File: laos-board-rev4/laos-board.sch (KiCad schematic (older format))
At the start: 101 parts, among them IC1 KB847, IC2 KB847, J1 USB-A, J10 I2C, J11 MBED NXP, J12 JP, J13 ZEXT, J14 ANALOG, J15 JP, J16 JP_3, J17 POLOLU1201, J18 YAXIS, J19 JP, J2 CAN, J20 YEXT, J21 JP, J22 JP_3, J23 POLOLU1201, J24 XAXIS, J25 JP, J26 XEXT, J27 OUTPUT, J28 VSENSOR, J29 INPUT12, J3 USBPWR, J30 JP, J31 JP_3, J32 POLOLU1201, J33 EAXIS, J34 INPUT34, J35 JP, J36 EEXT, J37 OUTPUT12, J38 VCPU, J39 OUTPUT34, J4 MAGJACK, J40 JP, J41 O1_SRC, J42 O2_SRC, J43 CONN_4, J44 JP, J5 CONN_3, J6 JP, J7 JP_3, J8 POLOLU1201, J9 ZAXIS, P1 FLATCONN, Q1 TIP115, Q2 TIP115, U1 65HVD251, U2 SDCARD, U3 7805, U4 MCP1703

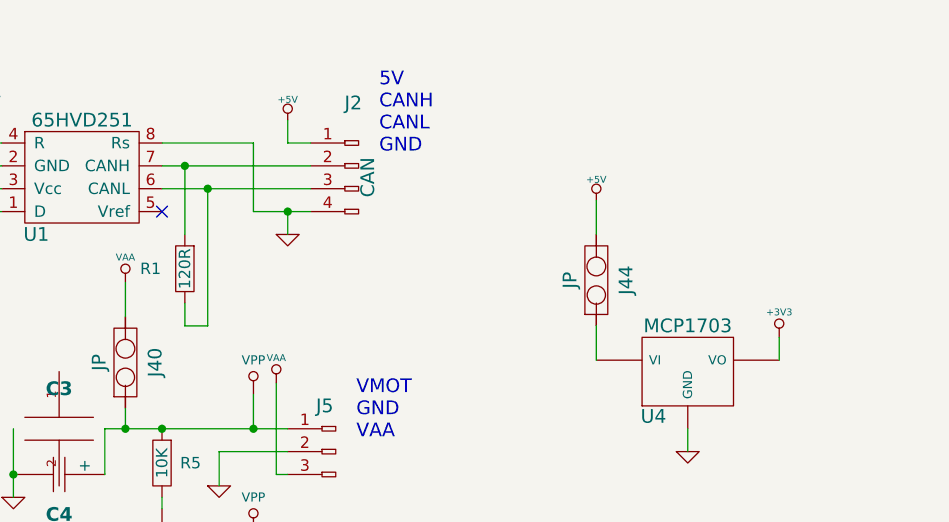
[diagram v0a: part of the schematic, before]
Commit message: added RJ12 for CAN
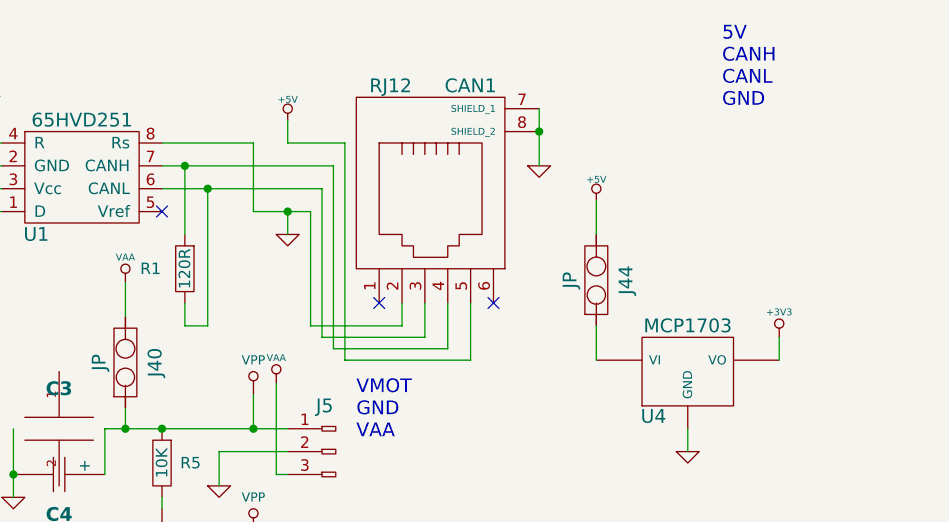
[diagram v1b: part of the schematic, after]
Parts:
- removed J2: CAN, Pkg, symbol CONN_4
- added CAN1: RJ12, symbol RJ12
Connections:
- net +5V: now also CAN1.5
- net GND: now also CAN1.2, CAN1.7 (SHIELD_1), CAN1.8 (SHIELD_2)
- net at R1.2, U1.7 (CANH): now also CAN1.4
- net at R1.1, U1.6 (CANL): now also CAN1.3
- no-connect marks 9 -> 11

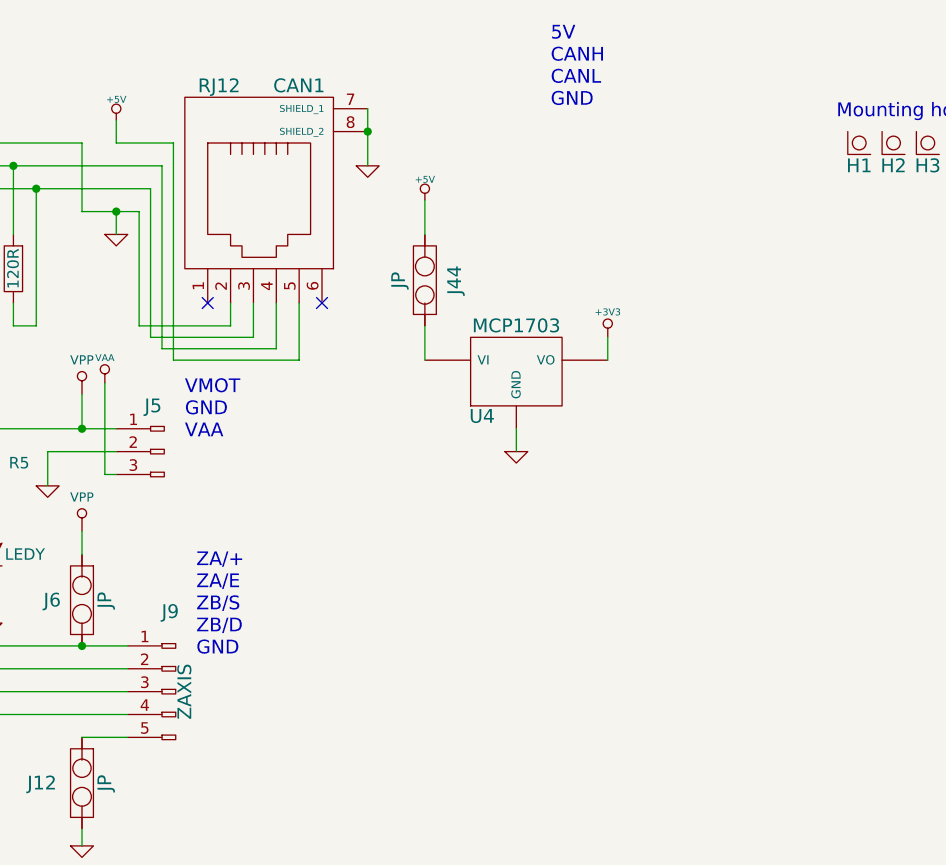
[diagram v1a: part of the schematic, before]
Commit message: updated CAN connector + thicker powerlines
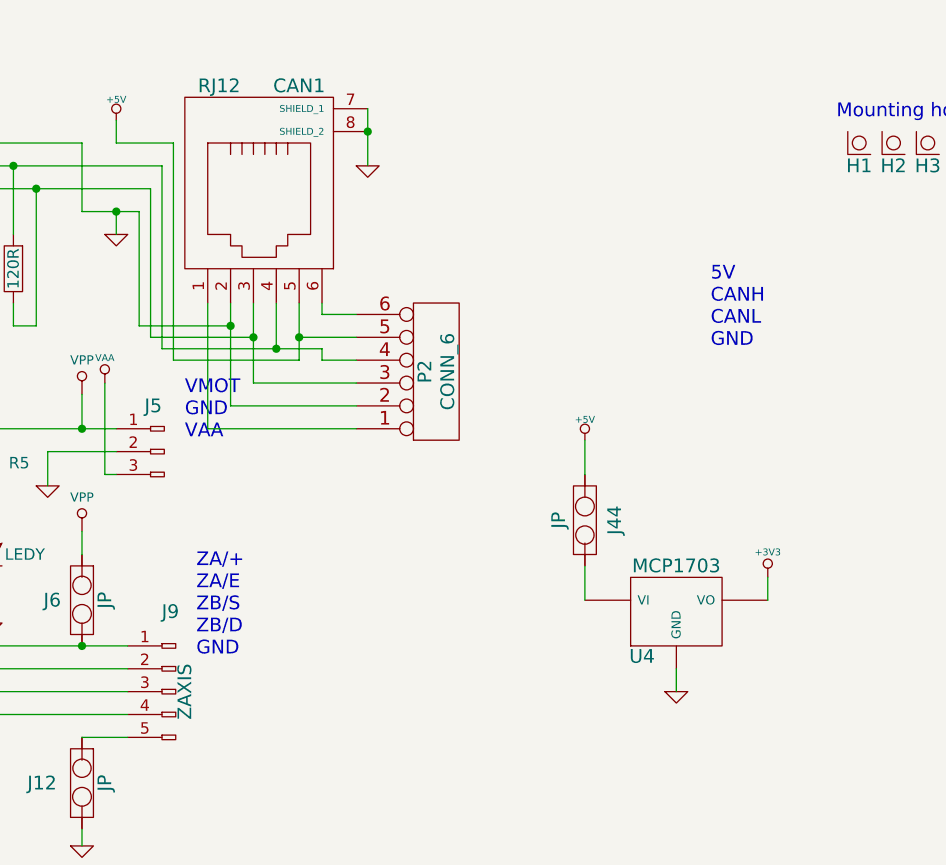
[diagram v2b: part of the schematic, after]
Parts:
- added P2: CONN_6, symbol CONN_6
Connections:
- net +5V: now also P2.5
- net GND: now also P2.2
- net at CAN1.3, R1.1, U1.6 (CANL): now also P2.3
- net at CAN1.4, R1.2, U1.7 (CANH): now also P2.4
- net at CAN1.1: now also P2.1
- net at CAN1.6: now also P2.6
- no-connect marks 11 -> 9
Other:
- moved on the sheet: J44, U4
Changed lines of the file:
@@
-EESchema Schematic File Version 2  date Sun 30 Sep 2012 06:13:09 PM CEST
+EESchema Schematic File Version 2  date Mon 01 Oct 2012 11:29:24 AM CEST
 LIBS:laos_kicad_lib
 LIBS:power
@@
 Sheet 1 1
 Title "LAOS"
-Date ""
+Date "1 oct 2012"
 Rev "4"
 Comp "http://www.laoslaser.org"
@@
 Comment4 ""
 $EndDescr
-NoConn ~ 13050 1500
-NoConn ~ 12550 1500
+Wire Wire Line
+	12550 1500 12550 2050
+Wire Wire Line
+	12550 2050 13200 2050
+Connection ~ 12950 1650
+Wire Wire Line
+	13200 1650 12950 1650
+Connection ~ 12750 1650
+Wire Wire Line
+	13200 1850 12750 1850
+Wire Wire Line
+	12750 1850 12750 1500
 Connection ~ 13250 750
 Wire Wire Line
@@
 	12400 800  12150 800
 Wire Wire Line
-	12750 1500 12750 1650
-Wire Wire Line
 	12750 1650 12300 1650
 Wire Wire Line
@@
 	12300 1000 11600 1000
 Wire Wire Line
-	13500 1600 13500 1750
-Wire Wire Line
-	14300 1750 14300 1650
-Wire Wire Line
-	13900 2050 13900 2150
+	14200 2650 14200 2800
+Wire Wire Line
+	15000 2800 15000 2700
+Wire Wire Line
+	14600 3100 14600 3200
 Wire Wire Line
 	6900 5300 6900 9975
@@
 	6700 5100 6600 5100
 Wire Wire Line
-	13500 1050 13500 1200
+	14200 2100 14200 2250
 Wire Wire Line
 	12250 1100 12250 1600
@@
 	12250 1600 12650 1600
 Wire Wire Line
-	12650 1600 12650 1500
-Wire Wire Line
-	12350 1700 12850 1700
-Wire Wire Line
 	12850 1700 12850 1500
+Wire Wire Line
+	13050 1500 13050 1550
+Wire Wire Line
+	13050 1550 13200 1550
+Wire Wire Line
+	12650 1500 12650 1950
+Wire Wire Line
+	12650 1950 13200 1950
+Connection ~ 12650 1600
+Wire Wire Line
+	12350 1700 13050 1700
+Wire Wire Line
+	13050 1700 13050 1750
+Wire Wire Line
+	13050 1750 13200 1750
+Connection ~ 12850 1700
+$Comp
+L CONN_6 P2
+U 1 1 506966F5
+P 13550 1800
+F 0 "P2" V 13500 1800 60  0000 C CNN
+F 1 "CONN_6" V 13600 1800 60  0000 C CNN
+	1    13550 1800
+	1    0    0    1
+$EndComp
 $Comp
 L GND #PWR01
@@
 L JP J44
 U 1 1 506860C5
-P 13500 1400
-F 0 "J44" H 13500 1270 60  0000 C CNN
-F 1 "JP" H 13500 1515 60  0000 C CNN
-	1    13500 1400
+P 14200 2450
+F 0 "J44" H 14200 2320 60  0000 C CNN
+F 1 "JP" H 14200 2565 60  0000 C CNN
+	1    14200 2450
 	0    -1   -1   0
 $EndComp
@@
 L GND #PWR02
 U 1 1 50686104
-P 13900 2150
-F 0 "#PWR02" H 13900 2150 30  0001 C CNN
-F 1 "GND" H 13900 2080 30  0001 C CNN
-	1    13900 2150
+P 14600 3200
+F 0 "#PWR02" H 14600 3200 30  0001 C CNN
+F 1 "GND" H 14600 3130 30  0001 C CNN
+	1    14600 3200
 	1    0    0    -1
 $EndComp
@@
 L MCP1703 U4
 U 1 1 506860E1
-P 13900 1750
-F 0 "U4" H 13750 1504 60  0000 C CNN
-F 1 "MCP1703" H 13900 1900 60  0000 C CNN
-	1    13900 1750
+P 14600 2800
+F 0 "U4" H 14450 2554 60  0000 C CNN
+F 1 "MCP1703" H 14600 2950 60  0000 C CNN
+	1    14600 2800
 	1    0    0    -1
 $EndComp
@@
 L +3V3 #PWR03
 U 1 1 50685E65
-P 14300 1650
-F 0 "#PWR03" H 14300 1610 30  0001 C CNN
-F 1 "+3V3" H 14300 1760 30  0000 C CNN
-	1    14300 1650
+P 15000 2700
+F 0 "#PWR03" H 15000 2660 30  0001 C CNN
+F 1 "+3V3" H 15000 2810 30  0000 C CNN
+	1    15000 2700
 	1    0    0    -1
 $EndComp
@@
 L +5V #PWR04
 U 1 1 50685366
-P 13500 1050
-F 0 "#PWR04" H 13500 1140 20  0001 C CNN
-F 1 "+5V" H 13500 1140 30  0000 C CNN
-	1    13500 1050
+P 14200 2100
+F 0 "#PWR04" H 14200 2190 20  0001 C CNN
+F 1 "+5V" H 14200 2190 30  0000 C CNN
+	1    14200 2100
 	1    0    0    -1
 $EndComp
@@
 	-1   0    0    1
 $EndComp
-Text Notes 14050 650  0    60   ~ 0
+Text Notes 14750 1700 0    60   ~ 0
 5V\nCANH\nCANL\nGND
 $Comp

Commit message: replaced 3v3 voltage regulator, added capacitors for Pololu decoupling
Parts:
- removed U4: MCP1703, symbol MCP1703
- added C10, C11, C9: 100uF, Pkg, symbol CAP_POL
- added C13, C14: 22nF, symbol CAP
- added U4: SP6205, symbol TPS769XX
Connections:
- net +3V3: now also C13.1, U4.5 (OUT)
- net GND: now also C10.2, C11.2, C13.2, C14.2, C9.2, U4.2 (GND)
- net VPP: now also C10.1 (+), C11.1 (+), C9.1 (+)
- net at J44.1: now also C14.1, U4.1 (IN)
- no-connect marks 9 -> 11
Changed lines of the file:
@@
-EESchema Schematic File Version 2  date Mon 01 Oct 2012 11:29:24 AM CEST
+EESchema Schematic File Version 2  date Tue 02 Oct 2012 08:27:16 PM CEST
 LIBS:laos_kicad_lib
 LIBS:power
@@
 Sheet 1 1
 Title "LAOS"
-Date "1 oct 2012"
+Date "2 oct 2012"
 Rev "4"
 Comp "http://www.laoslaser.org"
@@
 $EndDescr
 Wire Wire Line
+	10050 8025 10300 8025
+Wire Wire Line
+	10050 8625 10150 8625
+Wire Wire Line
+	10050 6800 10150 6800
+Connection ~ 10300 4450
+Wire Wire Line
+	10050 4450 10700 4450
+Wire Wire Line
+	10700 4450 10700 5150
+Wire Wire Line
+	10050 3400 10150 3400
+Connection ~ 14650 3350
+Connection ~ 15350 2800
+Wire Wire Line
+	15350 2700 15350 2850
+Wire Wire Line
+	13900 2850 13900 2800
+Wire Wire Line
 	12550 1500 12550 2050
 Wire Wire Line
@@
 Wire Wire Line
 	14200 2650 14200 2800
-Wire Wire Line
-	15000 2800 15000 2700
-Wire Wire Line
-	14600 3100 14600 3200
 Wire Wire Line
 	6900 5300 6900 9975
@@
 	11850 2150 12150 2150
 Wire Wire Line
-	10300 7850 10300 8025
+	10300 8025 10300 7850
 Wire Wire Line
 	12000 5900 12000 6000
@@
 	8250 8725 9300 8725
 Wire Wire Line
-	10050 8625 10150 8625
-Wire Wire Line
 	9200 8425 9300 8425
 Wire Wire Line
@@
 Connection ~ 8750 8325
 Wire Wire Line
-	10300 8025 10050 8025
-Wire Wire Line
 	10050 8125 10300 8125
 Wire Wire Line
@@
 Wire Wire Line
 	10300 6300 10050 6300
-Wire Wire Line
-	10050 6200 10300 6200
 Connection ~ 8750 6500
 Wire Wire Line
@@
 	8150 6400 8100 6400
 Wire Wire Line
-	10150 6100 10150 6800
+	10150 6800 10150 6100
 Wire Wire Line
 	9300 6600 9200 6600
-Wire Wire Line
-	10150 6800 10050 6800
 Wire Wire Line
 	9300 6700 9200 6700
@@
 	9200 4950 9300 4950
 Wire Wire Line
-	10050 5050 10150 5050
-Wire Wire Line
 	9200 4850 9300 4850
 Wire Wire Line
-	10150 5050 10150 4350
+	10150 4350 10150 5050
 Wire Wire Line
 	8150 4650 8100 4650
@@
 Connection ~ 8750 4750
 Wire Wire Line
-	10050 4450 10300 4450
-Wire Wire Line
 	10300 4450 10300 4350
 Wire Wire Line
@@
 	10300 2900 10050 2900
 Wire Wire Line
-	10300 2700 10300 2800
-Wire Wire Line
-	10300 2800 10050 2800
+	10300 2800 10300 2700
 Connection ~ 8750 3100
 Wire Wire Line
@@
 	8150 3000 8100 3000
 Wire Wire Line
-	10150 2700 10150 3400
+	10150 3400 10150 2700
 Wire Wire Line
 	9300 3200 9200 3200
-Wire Wire Line
-	10150 3400 10050 3400
 Wire Wire Line
 	9300 3300 9200 3300
@@
 	13050 1750 13200 1750
 Connection ~ 12850 1700
+Wire Wire Line
+	14200 2800 13900 2800
+Wire Wire Line
+	15350 2800 15100 2800
+Wire Wire Line
+	14650 3250 14650 3550
+Wire Wire Line
+	13900 3350 15350 3350
+Wire Wire Line
+	10700 3500 10700 2800
+Wire Wire Line
+	10700 2800 10050 2800
+Connection ~ 10300 2800
+Wire Wire Line
+	10150 5050 10050 5050
+Wire Wire Line
+	10700 6900 10700 6200
+Wire Wire Line
+	10700 6200 10050 6200
+Connection ~ 10300 6200
+$Comp
+L CAP C14
+U 1 1 506A9A61
+P 13900 3100
+F 0 "C14" V 14000 3250 50  0000 C CNN
+F 1 "22nF" V 14000 2950 50  0000 C CNN
+	1    13900 3100
+	1    0    0    -1
+$EndComp
+$Comp
+L CAP C13
+U 1 1 506A9A52
+P 15350 3100
+F 0 "C13" V 15450 3250 50  0000 C CNN
+F 1 "22nF" V 15450 2950 50  0000 C CNN
+	1    15350 3100
+	1    0    0    -1
+$EndComp
+NoConn ~ 15100 2950
+NoConn ~ 14200 2950
+$Comp
+L TPS769XX U4
+U 1 1 506A9571
+P 14650 2950
+F 0 "U4" H 14800 3250 60  0000 C CNN
+F 1 "SP6205" H 14950 2750 60  0000 C CNN
+	1    14650 2950
+	1    0    0    -1
+$EndComp
+$Comp
+L CAP_POL C9
+U 1 1 506AAD2D
+P 10500 3500
+F 0 "C9" H 10400 3550 60  0000 C CNB
+F 1 "100uF" H 10675 3425 60  0000 C CNN
+F 2 "Pkg" H 10500 3275 30  0000 C CNN
+	1    10500 3500
+	1    0    0    -1
+$EndComp
+$Comp
+L CAP_POL C10
+U 1 1 506AAD1E
+P 10500 5150
+F 0 "C10" H 10400 5200 60  0000 C CNB
+F 1 "100uF" H 10675 5075 60  0000 C CNN
+F 2 "Pkg" H 10500 4925 30  0000 C CNN
+	1    10500 5150
+	1    0    0    -1
+$EndComp
+$Comp
+L CAP_POL C11
+U 1 1 506AAD0F
+P 10500 6900
+F 0 "C11" H 10400 6950 60  0000 C CNB
+F 1 "100uF" H 10675 6825 60  0000 C CNN
+F 2 "Pkg" H 10500 6675 30  0000 C CNN
+	1    10500 6900
+	1    0    0    -1
+$EndComp
 $Comp
 L CONN_6 P2
@@
 L GND #PWR02
 U 1 1 50686104
-P 14600 3200
-F 0 "#PWR02" H 14600 3200 30  0001 C CNN
-F 1 "GND" H 14600 3130 30  0001 C CNN
-	1    14600 3200
-	1    0    0    -1
-$EndComp
-$Comp
-L MCP1703 U4
-U 1 1 506860E1
-P 14600 2800
-F 0 "U4" H 14450 2554 60  0000 C CNN
-F 1 "MCP1703" H 14600 2950 60  0000 C CNN
-	1    14600 2800
+P 14650 3550
+F 0 "#PWR02" H 14650 3550 30  0001 C CNN
+F 1 "GND" H 14650 3480 30  0001 C CNN
+	1    14650 3550
 	1    0    0    -1
 $EndComp
@@
 L +3V3 #PWR03
 U 1 1 50685E65
-P 15000 2700
-F 0 "#PWR03" H 15000 2660 30  0001 C CNN
-F 1 "+3V3" H 15000 2810 30  0000 C CNN
-	1    15000 2700
+P 15350 2700
+F 0 "#PWR03" H 15350 2660 30  0001 C CNN
+F 1 "+3V3" H 15350 2810 30  0000 C CNN
+	1    15350 2700
 	1    0    0    -1
 $EndComp
@@
 P 10500 9150
 F 0 "J36" H 10500 9375 60  0000 C CNN
-F 1 "EEXT" H 10450 8950 60  0000 C CNN
+F 1 "EEXT" H 10775 9000 60  0000 C CNN
 F 2 "Pkg" H 10600 8950 30  0001 C CNN
 	1    10500 9150
